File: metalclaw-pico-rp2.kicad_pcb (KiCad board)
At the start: 4 copper layers, 21 x 51 mm, 75 parts, among them J1 USB_C_Receptacle_USB2.0_14P, J2 Conn_01x05, J3 Conn_02x05_Odd_Even, J4 Conn_Coaxial, SW1 SW_Push, SW2 SW_Push, U1 ESP32-S2, U2 MX25L3236FM2I-08G-TR, U3 APS6404L-3SQRx-SN, U4 RP2350B, U5 XC6220B331MR, Y1 XRCGB40M000F1S2FR0

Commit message: Fill in BOM component details
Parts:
- removed the C19 at (157.1, 96.3)
- removed the C2 at (170.2, 92.5)
- removed J4: Conn_Coaxial, Connector_Coaxial:U.FL_Hirose_U.FL-R-SMT-1_Vertical
- removed the R17 at (157.8, 108.4)
- removed the R32 at (168.0, 116.1)
- removed the R33 at (166.6, 115.4)
- removed the R34 at (166.6, 116.7)
- removed the R35 at (168.0, 117.4)
- removed the R36 at (157.8, 110.5)
- removed the R37 at (170.2, 122.3)
- removed the R38 at (166.6, 118.1)
- removed the R39 at (157.7, 112.9)
- removed the R40 at (157.7, 115.2)
- removed U4: RP2350B, Package_DFN_QFN:QFN-80-1EP_10x10mm_P0.4mm_EP3.4x3.4mm
- added C14: 4.7u, Capacitor_SMD:C_0402_1005Metric, F.Cu at (196.6, 107.3)
- added C15: 100n, Capacitor_SMD:C_0201_0603Metric, F.Cu at (183.8, 99.7)
- added C22: 4.7u, Capacitor_SMD:C_0402_1005Metric, F.Cu at (196.6, 109.2)
- added C4: 1u, Capacitor_SMD:C_0201_0603Metric, F.Cu at (183.8, 87.5)
- added C5: 1u, Capacitor_SMD:C_0201_0603Metric, F.Cu at (183.8, 89.2)
- added C7: 1u, Capacitor_SMD:C_0201_0603Metric, F.Cu at (183.8, 91.0)
- added C8: 1u, Capacitor_SMD:C_0201_0603Metric, F.Cu at (183.8, 92.7)
- added C9: 1u, Capacitor_SMD:C_0201_0603Metric, F.Cu at (183.8, 94.5)
- added JP1: Jumper_2_Bridged, Jumper:SolderJumper-2_P1.3mm_Bridged2Bar_Pad1.0x1.5mm, F.Cu at (197.4, 112.0)
- added R1: 5.1k, Resistor_SMD:R_0201_0603Metric, F.Cu at (186.2, 87.5)
- added R10: 5.1k, Resistor_SMD:R_0201_0603Metric, F.Cu at (188.7, 87.5)
- added R11: 5.1k, Resistor_SMD:R_0201_0603Metric, F.Cu at (188.7, 89.2)
- added R12: 5.1k, Resistor_SMD:R_0201_0603Metric, F.Cu at (188.7, 91.0)
- added R13: 5.1k, Resistor_SMD:R_0201_0603Metric, F.Cu at (188.7, 92.7)
- added R14: 5.1k, Resistor_SMD:R_0201_0603Metric, F.Cu at (188.7, 94.5)
- added R15: 5.1k, Resistor_SMD:R_0201_0603Metric, F.Cu at (188.7, 96.2)
- added R18: 5.1k, Resistor_SMD:R_0201_0603Metric, F.Cu at (188.7, 99.7)
- added R2: 5.1k, Resistor_SMD:R_0201_0603Metric, F.Cu at (186.2, 89.2)
- added R20: 5.1k, Resistor_SMD:R_0201_0603Metric, F.Cu at (188.7, 101.5)
- added R21: 5.1k, Resistor_SMD:R_0201_0603Metric, F.Cu at (191.1, 87.5)
- added R22: 5.1k, Resistor_SMD:R_0201_0603Metric, F.Cu at (191.1, 89.2)
- added R23: 5.1k, Resistor_SMD:R_0201_0603Metric, F.Cu at (191.1, 91.0)
- added R24: 5.1k, Resistor_SMD:R_0201_0603Metric, F.Cu at (191.1, 92.7)
- added R25: 5.1k, Resistor_SMD:R_0201_0603Metric, F.Cu at (191.1, 94.5)
- added R26: 5.1k, Resistor_SMD:R_0201_0603Metric, F.Cu at (191.1, 96.2)
- added R27: 5.1k, Resistor_SMD:R_0201_0603Metric, F.Cu at (191.1, 98.0)
- added R29: 5.1k, Resistor_SMD:R_0201_0603Metric, F.Cu at (191.1, 101.5)
- added R3: 5.1k, Resistor_SMD:R_0201_0603Metric, F.Cu at (186.2, 91.0)
- added R4: 5.1k, Resistor_SMD:R_0201_0603Metric, F.Cu at (186.2, 92.7)
- added R5: 5.1k, Resistor_SMD:R_0201_0603Metric, F.Cu at (186.2, 94.5)
- added R55: 220, Resistor_SMD:R_0201_0603Metric, F.Cu at (193.6, 91.0)
- added R56: 220, Resistor_SMD:R_0201_0603Metric, F.Cu at (193.6, 92.7)
- added R57: 220, Resistor_SMD:R_0201_0603Metric, F.Cu at (193.6, 94.5)
- added R58: 220, Resistor_SMD:R_0201_0603Metric, F.Cu at (193.6, 96.2)
- added R59: 220, Resistor_SMD:R_0201_0603Metric, F.Cu at (193.6, 98.0)
- added R6: 5.1k, Resistor_SMD:R_0201_0603Metric, F.Cu at (186.2, 96.2)
- added R60: 220, Resistor_SMD:R_0201_0603Metric, F.Cu at (193.6, 99.7)
- added R61: 220, Resistor_SMD:R_0201_0603Metric, F.Cu at (193.6, 101.5)
- added R62: 220, Resistor_SMD:R_0201_0603Metric, F.Cu at (196.0, 87.5)
- added R63: 220, Resistor_SMD:R_0201_0603Metric, F.Cu at (196.0, 89.2)
- added R64: 220, Resistor_SMD:R_0201_0603Metric, F.Cu at (196.0, 91.0)
- added R65: 220, Resistor_SMD:R_0201_0603Metric, F.Cu at (196.0, 92.7)
- added R66: 220, Resistor_SMD:R_0201_0603Metric, F.Cu at (196.0, 94.5)
- added R67: 220, Resistor_SMD:R_0201_0603Metric, F.Cu at (196.0, 96.2)
- added R68: 220, Resistor_SMD:R_0201_0603Metric, F.Cu at (196.0, 98.0)
- added R69: 220, Resistor_SMD:R_0201_0603Metric, F.Cu at (196.0, 99.7)
- added R7: 5.1k, Resistor_SMD:R_0201_0603Metric, F.Cu at (186.2, 98.0)
- added R70: 220, Resistor_SMD:R_0201_0603Metric, F.Cu at (196.0, 101.5)
- added R71: 220, Resistor_SMD:R_0201_0603Metric, F.Cu at (198.5, 87.5)
- added R72: 220, Resistor_SMD:R_0201_0603Metric, F.Cu at (198.5, 89.2)
- added R73: 220, Resistor_SMD:R_0201_0603Metric, F.Cu at (198.5, 91.0)
- added R74: 220, Resistor_SMD:R_0201_0603Metric, F.Cu at (198.5, 92.7)
- added R75: 220, Resistor_SMD:R_0201_0603Metric, F.Cu at (198.5, 94.5)
- added R76: 220, Resistor_SMD:R_0201_0603Metric, F.Cu at (198.5, 96.2)
- added R79: 33, Resistor_SMD:R_0402_1005Metric, F.Cu at (199.5, 106.7)
- added R80: 5.1k, Resistor_SMD:R_0201_0603Metric, F.Cu at (198.5, 98.0)
- added R81: 5.1k, Resistor_SMD:R_0201_0603Metric, F.Cu at (198.5, 99.7)
- added R82: 5.1k, Resistor_SMD:R_0201_0603Metric, F.Cu at (198.5, 101.5)
- added R9: 5.1k, Resistor_SMD:R_0201_0603Metric, F.Cu at (186.2, 101.5)
- C11: value 1u -> 100n; footprint Capacitor_SMD:C_0201_0603Metric -> Capacitor_SMD:C_0402_1005Metric
- C12: value C -> 1u
- C13: value C -> 4.7u; footprint Capacitor_SMD:C_0201_0603Metric -> Capacitor_SMD:C_0402_1005Metric
- C16: value 1u -> 100n
- C24: renamed from C5; value 6p -> 15p; footprint Capacitor_SMD:C_0201_0603Metric -> Capacitor_SMD:C_0402_1005Metric
- C25: renamed from C6; value 6p -> 15p; footprint Capacitor_SMD:C_0201_0603Metric -> Capacitor_SMD:C_0402_1005Metric
- L1: value L -> 3.3u; footprint Inductor_SMD:L_0201_0603Metric -> Inductor_SMD_Wurth:L_Wurth_WE-LQSH-2010
- R16, R28, R8: value 220 -> 5.1k
- U2: value MX25L3236FM2I-08G-TR -> RP2354B; footprint Package_SO:SOIC-8_5.3x5.3mm_P1.27mm -> Package_DFN_QFN:QFN-80-1EP_10x10mm_P0.4mm_EP3.4x3.4mm
- Y1: value XRCGB40M000F1S2FR0 -> ABM8-272-T3; footprint Crystal:Crystal_SMD_2016-4Pin_2.0x1.6mm -> Crystal:Crystal_SMD_3225-4Pin_3.2x2.5mm
- moved R31 49.1 mm to (193.6, 89.2)
- moved L1 34.8 mm to (200.0, 104.0), turned to 0 degrees
- moved C11 33.9 mm to (196.6, 103.3), turned to 0 degrees
- moved C13 30.3 mm to (196.6, 105.3), turned to 0 degrees
- moved U2 30.2 mm to (189.1, 108.5), turned to 0 degrees
- moved R30 26.0 mm to (193.6, 87.5), turned to 0 degrees
- moved R28 22.0 mm to (191.1, 99.7)
- moved C12 21.5 mm to (183.8, 98.0), turned to 0 degrees
- moved C10 19.9 mm to (183.8, 96.2), turned to 0 degrees
- moved C16 18.8 mm to (183.8, 101.5), turned to 0 degrees
- moved R16 18.4 mm to (188.7, 98.0), turned to 0 degrees
- moved R8 15.9 mm to (186.2, 99.7), turned to 0 degrees
- renumbered A2 to A1, C15 to C17, C14 to C18, C9 to C19, C3 to C2, C8 to C20, C7 to C21, C4 to C23, C18 to C26, C17 to C6, J3 to J2, R41 to R17, R42 to R19, R2 to R32, R3 to R33, R4 to R34, R5 to R35, R6 to R36, R7 to R37, R18 to R38, R19 to R39, R20 to R40, R21 to R41, R22 to R42, R23 to R43, R24 to R44, R25 to R45, R26 to R46, R27 to R47, R15 to R48, R14 to R49, R13 to R50, R12 to R51, R11 to R52, R10 to R53, R9 to R54, R1 to R77, R29 to R78, SW2 to SW1, SW1 to SW2, U5 to U1
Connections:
- A1 pad 1: Net-(A2-GPIO0) -> /GP0
- A1 pad 10: Net-(A2-GPIO7) -> /GP7
- A1 pad 11: Net-(A2-GPIO8) -> /GP8
- A1 pad 12: Net-(A2-GPIO9) -> /GP9
- A1 pad 14: Net-(A2-GPIO10) -> /GP10
- A1 pad 15: Net-(A2-GPIO11) -> /GP11
- A1 pad 16: Net-(A2-GPIO12) -> /GP12
- A1 pad 17: Net-(A2-GPIO13) -> /GP13
- A1 pad 19: Net-(A2-GPIO14) -> /GP14
- A1 pad 2: Net-(A2-GPIO1) -> /GP1
- A1 pad 20: Net-(A2-GPIO15) -> /GP15
- A1 pad 21: Net-(A2-GPIO16) -> /GP16
- A1 pad 22: Net-(A2-GPIO17) -> /GP17
- A1 pad 24: Net-(A2-GPIO18) -> /GP18
- A1 pad 25: Net-(A2-GPIO19) -> /GP19
- A1 pad 26: Net-(A2-GPIO20) -> /GP20
- A1 pad 27: Net-(A2-GPIO21) -> /GP21
- A1 pad 29: Net-(A2-GPIO22) -> /GP22
- A1 pad 31: Net-(A2-GPIO26_ADC0) -> Net-(A1-GPIO26_ADC0)
- A1 pad 32: Net-(A2-GPIO27_ADC1) -> Net-(A1-GPIO27_ADC1)
- A1 pad 33: GND -> Net-(A1-AGND)
- A1 pad 34: /GP28 -> Net-(A1-GPIO28_ADC2)
- A1 pad 35: +3V3 -> unconnected-(A1-ADC_VREF-Pad35)
- A1 pad 36: unconnected-(A2-3V3-Pad36) -> +3.3VP
- A1 pad 39: unconnected-(A2-VSYS-Pad39) -> VS
- A1 pad 4: Net-(A2-GPIO2) -> /GP2
- A1 pad 40: VBUS -> unconnected-(A1-VBUS-Pad40)
- A1 pad 5: Net-(A2-GPIO3) -> /GP3
- A1 pad 6: Net-(A2-GPIO4) -> /GP4
- A1 pad 7: Net-(A2-GPIO5) -> /GP5
- A1 pad 9: Net-(A2-GPIO6) -> /GP6
- C10 pad 1: +3V3 -> GND
- C10 pad 2: GND -> Net-(C10-Pad2)
- C11 pad 1: +3V3 -> GND
- C11 pad 2: GND -> Net-(U2-VREG_AVDD)
- C12 pad 1: Net-(U1-LNA_IN) -> GND
- C12 pad 2: GND -> +3V3
- C13 pad 1: Net-(J4-In) -> GND
- C13 pad 2: GND -> +3V3
- C16 pad 1: Net-(C16-Pad1) -> GND
- C16 pad 2: /3V3_EN -> +3V3
- C17 pad 1: +3V3 -> GND
- C17 pad 2: GND -> +3V3
- C18 pad 1: +3V3 -> GND
- C18 pad 2: GND -> +3V3
- C19 pad 1: +3V3 -> GND
- C19 pad 2: GND -> +3V3
- C20 pad 1: +3V3 -> GND
- C20 pad 2: GND -> +3V3
- C21 pad 1: +3V3 -> GND
- C21 pad 2: GND -> Net-(U2-VREG_FB)
- C23 pad 1: +3V3 -> GND
- C23 pad 2: GND -> +3V3
- C24 pad 1: Net-(U1-XTAL_P) -> Net-(U2-XIN)
- C25 pad 1: Net-(U1-XTAL_N) -> GND
- C25 pad 2: GND -> Net-(U2-XOUT)
- C26 pad 1: GND -> +3V3
- C26 pad 2: VDD -> GND
- C6 pad 1: Net-(C17-Pad1) -> GND
- J1 pad A6: /USB_D+ -> Net-(J1-D+-PadA6)
- J1 pad A7: /USB_D- -> Net-(J1-D--PadA7)
- J1 pad B6: /USB_D+ -> Net-(J1-D+-PadA6)
- J1 pad B7: /USB_D- -> Net-(J1-D--PadA7)
- J1 pad S1: unconnected-(J1-SHIELD-PadS1) -> GND
- J2 pad 10: unconnected-(J3-Pin_10-Pad10) -> /RESET
- J2 pad 2: /MTMS -> Net-(J2-Pin_2)
- J2 pad 4: /MTCK -> Net-(J2-Pin_4)
- J2 pad 6: /MTDO -> unconnected-(J2-Pin_6-Pad6)
- J2 pad 7: GND -> unconnected-(J2-Pin_7-Pad7)
- J2 pad 8: /MTDI -> unconnected-(J2-Pin_8-Pad8)
- L1 pad 1: Net-(U1-LNA_IN) -> Net-(U2-VREG_FB)
- L1 pad 2: Net-(J4-In) -> Net-(U2-VREG_LX)
- R16 pad 1: Net-(A2-GPIO27_ADC1) -> +3.3VP
- R16 pad 2: /GP27 -> /GP8
- R17 pad 2: /3V3_EN -> /BOOTSEL
- R28 pad 1: Net-(U1-GPIO21) -> /GP16
- R28 pad 2: /GP28 -> +3.3VP
- R30 pad 1: GND -> /GP27
- R30 pad 2: /RUN -> Net-(C9-Pad2)
- R31 pad 1: GND -> /GP28
- R31 pad 2: /GP15 -> Net-(C10-Pad2)
- R32 pad 1: Net-(A2-GPIO0) -> /GP3
- R32 pad 2: /GP0 -> Net-(U2-GPIO0)
- R33 pad 1: Net-(A2-GPIO1) -> /3V3_EN
- R33 pad 2: /GP1 -> Net-(U2-GPIO1)
- R34 pad 1: Net-(A2-GPIO2) -> /GP1
- R34 pad 2: /GP2 -> Net-(U2-GPIO2)
- R35 pad 1: Net-(A2-GPIO3) -> /GP0
- R35 pad 2: /GP3 -> Net-(U2-GPIO3)
- R36 pad 1: Net-(A2-GPIO4) -> /GP0
- R36 pad 2: /GP4 -> Net-(U2-GPIO4)
- R37 pad 1: Net-(A2-GPIO5) -> /GP1
- R37 pad 2: /GP5 -> Net-(U2-GPIO5)
- R38 pad 1: Net-(A2-GPIO6) -> /GP2
- R38 pad 2: /GP6 -> Net-(U2-GPIO6)
- R39 pad 1: Net-(A2-GPIO7) -> /GP3
- R39 pad 2: /GP7 -> Net-(U2-GPIO7)
- R40 pad 1: Net-(A2-GPIO8) -> /GP7
- R40 pad 2: /GP8 -> Net-(U2-GPIO8)
- R41 pad 1: Net-(A2-GPIO9) -> /RUN
- R41 pad 2: /GP9 -> Net-(U2-GPIO9)
- R42 pad 1: Net-(A2-GPIO10) -> /GP5
- R42 pad 2: /GP10 -> Net-(U2-GPIO10)
- R43 pad 1: Net-(A2-GPIO11) -> /GP4
- R43 pad 2: /GP11 -> Net-(U2-GPIO11)
- R44 pad 1: Net-(A2-GPIO12) -> /GP4
- R44 pad 2: /GP12 -> Net-(U2-GPIO12)
- R45 pad 1: Net-(A2-GPIO13) -> /GP5
- R45 pad 2: /GP13 -> Net-(U2-GPIO13)
- R46 pad 1: Net-(A2-GPIO14) -> /GP6
- R46 pad 2: /GP14 -> Net-(U2-GPIO14)
- R47 pad 1: Net-(A2-GPIO15) -> /GP7
- R47 pad 2: /GP15 -> Net-(U2-GPIO15)
- R48 pad 1: Net-(A2-GPIO16) -> /GP11
- R48 pad 2: /GP16 -> Net-(U2-GPIO16)
- R49 pad 1: Net-(A2-GPIO17) -> /SWCLK
- R49 pad 2: /GP17 -> Net-(U2-GPIO17)
- R50 pad 1: Net-(A2-GPIO18) -> /GP9
- R50 pad 2: /GP18 -> Net-(U2-GPIO18)
- R51 pad 1: Net-(A2-GPIO19) -> /GP8
- R51 pad 2: /GP19 -> Net-(U2-GPIO19)
- R52 pad 1: Net-(A2-GPIO20) -> /GP8
- R52 pad 2: /GP20 -> Net-(U2-GPIO20)
- R53 pad 1: Net-(A2-GPIO21) -> /GP9
- R53 pad 2: /GP21 -> Net-(U2-GPIO21)
- R54 pad 1: Net-(A2-GPIO22) -> /GP10
- R54 pad 2: /GP22 -> Net-(U2-GPIO22)
- R8 pad 1: Net-(A2-GPIO26_ADC0) -> +3.3VP
- R8 pad 2: /GP26 -> /GP12
- SW1 pad 2: Net-(C16-Pad1) -> Net-(R80-Pad2)
- SW2 pad 2: Net-(C17-Pad1) -> /RESET
- U2 pad 1: Net-(U1-SPICS0) -> Net-(U2-GPIO4)
- U2 pad 2: Net-(U1-SPIQ) -> Net-(U2-GPIO5)
- U2 pad 3: Net-(U1-SPIWP) -> Net-(U2-GPIO6)
- U2 pad 4: GND -> Net-(U2-GPIO7)
- U2 pad 5: Net-(U1-SPID) -> +3V3
- U2 pad 6: Net-(U1-SPICLK) -> Net-(U2-GPIO8)
- U2 pad 7: Net-(U1-SPIHD) -> Net-(U2-GPIO9)
- U2 pad 8: VDD -> Net-(U2-GPIO10)
- U3 pad 1: Net-(U1-SPICS1) -> Net-(U2-GPIO47/ADC7)
- U3 pad 2: Net-(U1-SPIQ) -> Net-(U2-QSPI_SD1)
- U3 pad 3: Net-(U1-SPIWP) -> Net-(U2-QSPI_SD2)
- U3 pad 5: Net-(U1-SPID) -> Net-(U2-QSPI_SD0)
- U3 pad 6: Net-(U1-SPICLK) -> Net-(U2-QSPI_SCLK)
- U3 pad 7: Net-(U1-SPIHD) -> Net-(U2-QSPI_SD3)
- U3 pad 8: VDD -> +3V3
- Y1 pad 1: Net-(U1-XTAL_N) -> Net-(U2-XIN)
- Y1 pad 3: Net-(U1-XTAL_P) -> Net-(U2-XOUT)
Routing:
- net (no net): track 0.00 -> 52.2 mm
- net Net-(U2-GPIO0): track 0.00 -> 46.5 mm, vias 0 -> 2
- net /GP0: track 49.6 -> 3.10 mm, vias 2 -> 0
- net Net-(J1-D--PadA7): track 0.00 -> 15.3 mm, vias 0 -> 1
- net /USB_D-: track 15.3 -> 0.00 mm, vias 1 -> 0
- net Net-(J1-D+-PadA6): track 0.00 -> 14.6 mm, vias 0 -> 1
- net /USB_D+: track 14.6 -> 0.00 mm, vias 1 -> 0
- net /GP21: track 13.8 -> 20.9 mm
- net Net-(A2-GPIO21): track 7.11 -> 0.00 mm
- net Net-(A2-GPIO17): track 5.36 -> 0.00 mm
- net Net-(U2-GPIO22): track 0.00 -> 4.87 mm, vias 0 -> 2
- net /GP22: track 7.84 -> 2.98 mm, vias 2 -> 0
- net Net-(A1-GPIO28_ADC2): track 0.00 -> 4.80 mm
- net /GP28: track 4.80 -> 0.00 mm
- net Net-(A2-GPIO14): track 4.16 -> 0.00 mm
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
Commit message: Rip out outdated footprints from layout
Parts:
- removed the J2 at (158.7, 120.2)
- removed the U1 at (163.8, 102.7)
- added C27: 100n, Capacitor_SMD:C_0402_1005Metric, F.Cu at (211.9, 108.4)
- added C28: 100n, Capacitor_SMD:C_0402_1005Metric, F.Cu at (211.9, 110.4)
- added C3: 100n, Capacitor_SMD:C_0402_1005Metric, F.Cu at (211.9, 106.5)
- added D1: PMEG2010ER,115, Diode_SMD:Nexperia_CFP3_SOD-123W, F.Cu at (216.1, 107.1)
- added R83: 1k, Resistor_SMD:R_0402_1005Metric, F.Cu at (214.8, 109.7)
- C10, C8, C9: value 1u -> 10n; footprint Capacitor_SMD:C_0201_0603Metric -> Capacitor_SMD:C_0402_1005Metric
- C11: value 100n -> 4.7u
- C12, C15, C16, C17, C18, C19, C20, C21, C23, C26: footprint Capacitor_SMD:C_0201_0603Metric -> Capacitor_SMD:C_0402_1005Metric
- C4, C5, C7: value 1u -> 1.5n; footprint Capacitor_SMD:C_0201_0603Metric -> Capacitor_SMD:C_0402_1005Metric
- C6: value 1u -> 100n; footprint Capacitor_SMD:C_0201_0603Metric -> Capacitor_SMD:C_0402_1005Metric
- J1: value USB_C_Receptacle_USB2.0_14P -> USB4105-GF-A
- J2: value Conn_02x05_Odd_Even -> FTSH-105-01-L-DV-K
- R1, R10, R11, R12, R13, R14, R15, R16, R17, R18, R19, R2, R20, R21, R24, R26, R27, R28, R3, R4, R5, R6, R7, R77, R78, R8, R9: footprint Resistor_SMD:R_0201_0603Metric -> Resistor_SMD:R_0402_1005Metric
- R22, R23, R25: value 5.1k -> 2.2k; footprint Resistor_SMD:R_0201_0603Metric -> Resistor_SMD:R_0402_1005Metric
- R29, R30, R31: value 5.1k -> 330; footprint Resistor_SMD:R_0201_0603Metric -> Resistor_SMD:R_0402_1005Metric
- R32, R34, R35, R36, R37, R38, R39, R40, R42, R43, R44, R45, R46, R47, R48, R49, R50, R51, R52, R53, R54, R55, R56, R57, R58, R59, R60, R61, R62, R63, R64, R65, R66, R67, R68, R69, R70, R71, R72, R73, R74, R75: value 220 -> 33; footprint Resistor_SMD:R_0201_0603Metric -> Resistor_SMD:R_0402_1005Metric
- R33, R41: value 220 -> 1k; footprint Resistor_SMD:R_0201_0603Metric -> Resistor_SMD:R_0402_1005Metric
- R76: value 220 -> 10k; footprint Resistor_SMD:R_0201_0603Metric -> Resistor_SMD:R_0402_1005Metric
- R80: value 5.1k -> 1k; footprint Resistor_SMD:R_0201_0603Metric -> Resistor_SMD:R_0402_1005Metric
- R81, R82: value 5.1k -> 27; footprint Resistor_SMD:R_0201_0603Metric -> Resistor_SMD:R_0402_1005Metric
- SW1, SW2: value SW_Push -> PTS810SJM250SMTR LFS
- U1: value XC6220B331MR -> XC6220B331MR-G
- U3: value APS6404L-3SQRx-SN -> APS6404L-3SQR-SN
- moved C18 41.5 mm to (125.6, 106.0)
- moved C21 41.5 mm to (124.4, 95.6)
- moved R17 41.5 mm to (129.1, 85.0)
- moved R36 41.5 mm to (115.6, 85.3)
- moved R38 41.5 mm to (115.6, 93.0)
- moved R43 41.5 mm to (115.6, 108.8)
- moved R49 41.5 mm to (127.1, 116.4)
- moved R50 41.5 mm to (128.5, 115.9)
- moved R51 41.5 mm to (128.5, 115.0)
- moved R53 41.5 mm to (127.1, 113.7)
- moved R54 41.5 mm to (129.1, 100.6)
- moved C17 41.5 mm to (116.9, 104.9)
- moved C20 41.5 mm to (117.3, 98.4)
- moved C24 41.5 mm to (120.9, 107.8)
- moved C26 41.5 mm to (116.3, 88.5)
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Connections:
- C1 pad 1: VBUS -> VS
- C25 pad 2: Net-(U2-XOUT) -> Net-(C25-Pad2)
- J1 pad A4: VBUS -> Net-(D1-A)
- J1 pad A9: VBUS -> Net-(D1-A)
- J1 pad B4: VBUS -> Net-(D1-A)
- J1 pad B9: VBUS -> Net-(D1-A)
- U1 pad 1: VBUS -> VS
- U1 pad 3: VBUS -> VS
- Y1 pad 3: Net-(U2-XOUT) -> Net-(C25-Pad2)
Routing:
- net (no net): track 52.2 -> 0.00 mm
- net /GP3: track 48.3 -> 0.00 mm, vias 4 -> 0
- net /GP4: track 47.8 -> 0.00 mm, vias 4 -> 0
- net /GP1: track 47.0 -> 0.00 mm, vias 2 -> 0
- net Net-(U2-GPIO0): track 46.5 -> 0.00 mm, vias 2 -> 0
- net /GP2: track 43.8 -> 0.00 mm, vias 2 -> 0
- net /GP7: track 37.7 -> 0.00 mm, vias 4 -> 0
- net /GP6: track 36.9 -> 0.00 mm, vias 4 -> 0
- net /GP5: track 34.6 -> 0.00 mm, vias 4 -> 0
- net /RUN: track 33.3 -> 0.00 mm, vias 1 -> 0
- net /GP8: track 31.1 -> 0.00 mm, vias 4 -> 0
- net /GP16: track 23.2 -> 0.00 mm, vias 1 -> 0
- net /GP18: track 21.2 -> 0.00 mm, vias 2 -> 0
- net /GP21: track 20.9 -> 0.00 mm, vias 1 -> 0
- net /GP17: track 18.0 -> 0.00 mm, vias 2 -> 0
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
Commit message: Switch to smaller footprints
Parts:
- C10, C15, C16, C17, C18, C19, C20, C21, C23, C24, C25, C27, C28, C3, C6, C8, C9: footprint Capacitor_SMD:C_0402_1005Metric -> Capacitor_SMD:C_0201_0603Metric
- JP1: moved to B.Cu
- R1, R10, R11, R12, R13, R14, R15, R16, R17, R18, R19, R2, R20, R21, R22, R23, R24, R25, R26, R27, R28, R29, R3, R30, R31, R33, R4, R41, R5, R6, R7, R76, R77, R78, R8, R80, R81, R82, R83, R9: footprint Resistor_SMD:R_0402_1005Metric -> Resistor_SMD:R_0201_0603Metric
- R32, R34, R35, R36, R37, R38, R39, R40, R42, R43, R44, R45, R46, R47, R48, R49, R50, R51, R52, R53, R54, R55, R56, R57, R58, R59, R60, R61, R62, R63, R64, R65, R66, R67, R68, R69, R70, R71, R72, R73, R74, R75: value 33 -> 100; footprint Resistor_SMD:R_0402_1005Metric -> Resistor_SMD:R_0201_0603Metric
- moved D1 54.9 mm to (170.1, 77.2), turned to 90 degrees
- moved R36 43.0 mm to (157.6, 76.1), turned to 0 degrees
- moved R35 42.8 mm to (157.6, 75.1), turned to 0 degrees
- moved R15 38.2 mm to (157.6, 74.1)
- moved U2 27.3 mm to (163.7, 98.3)
- moved J2 24.6 mm to (163.6, 116.4)
- turned JP1 to 180 degrees

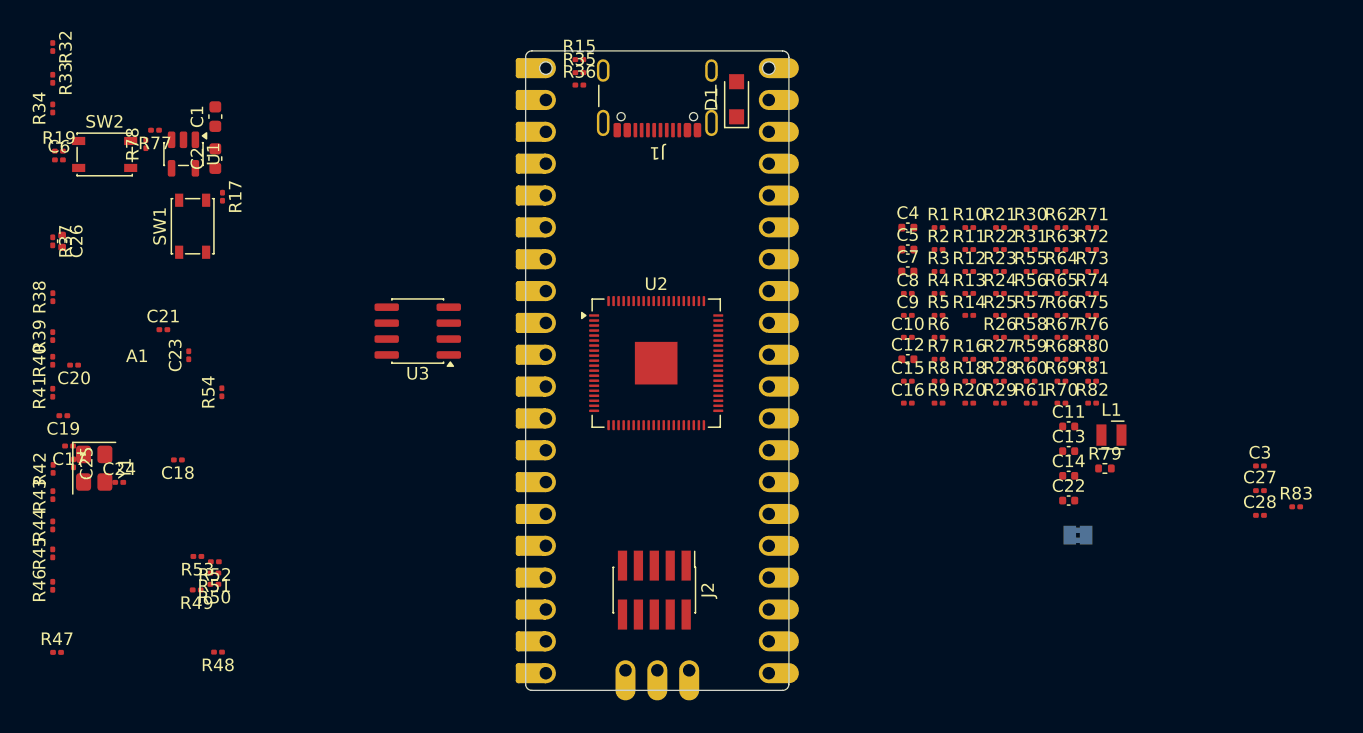
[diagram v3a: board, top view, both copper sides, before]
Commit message: Move resistors to their rough placements
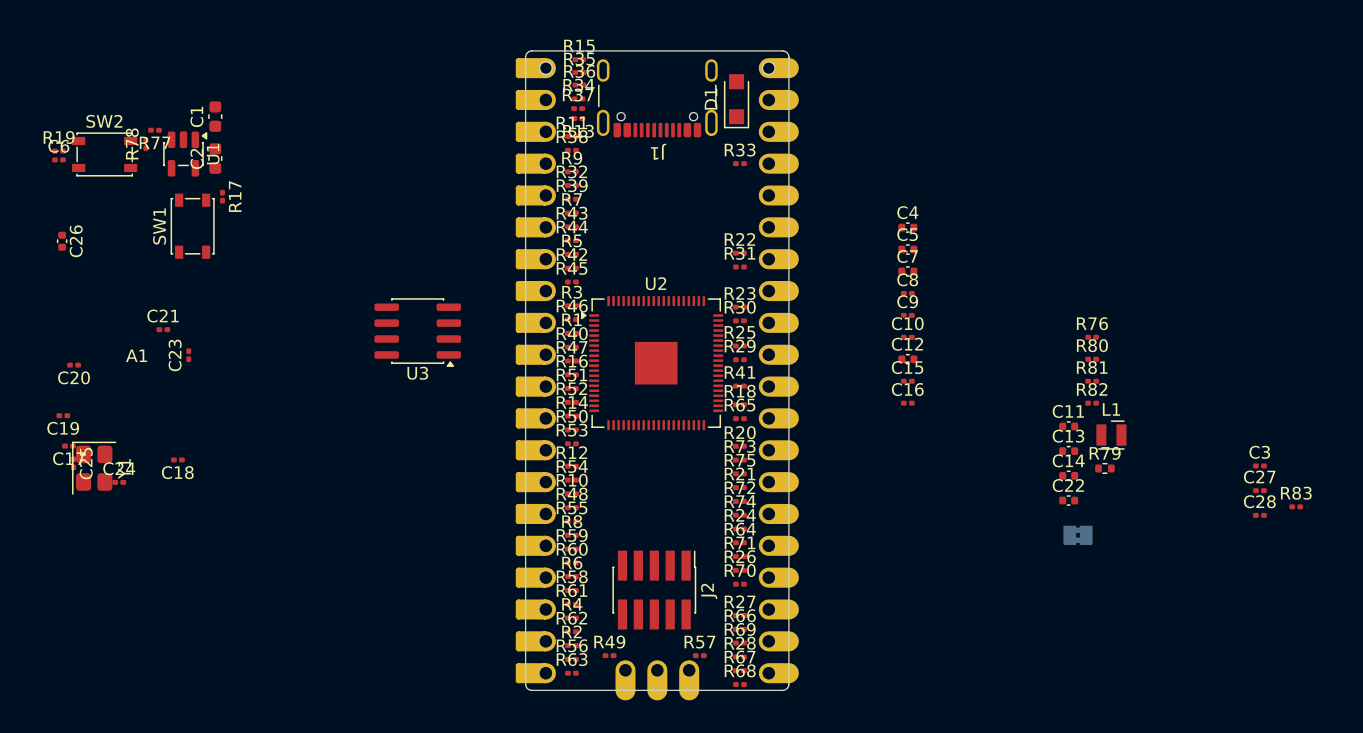
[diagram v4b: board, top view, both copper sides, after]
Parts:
- moved R33 55.2 mm to (170.4, 82.4), turned to 0 degrees
- moved R41 54.8 mm to (170.4, 100.1), turned to 0 degrees
- moved R63 51.6 mm to (157.0, 123.0)
- moved R62 50.6 mm to (157.0, 119.7)
- moved R44 47.2 mm to (157.0, 88.5), turned to 0 degrees
- moved R47 47.2 mm to (157.0, 98.1)
- moved R56 46.8 mm to (157.0, 121.9)
- moved R45 46.7 mm to (157.0, 91.8), turned to 0 degrees
- moved R43 46.6 mm to (157.0, 87.4), turned to 0 degrees
- moved R46 46.5 mm to (157.0, 94.8), turned to 0 degrees
- moved R42 44.4 mm to (157.0, 90.7), turned to 0 degrees
- moved R37 43.2 mm to (157.5, 78.0), turned to 0 degrees
- moved R2 43.0 mm to (157.0, 120.8)
- moved R38 43.0 mm to (157.0, 81.3), turned to 0 degrees
- moved R32 42.9 mm to (157.0, 84.1), turned to 0 degrees
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
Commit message: Move more components to their rough placements
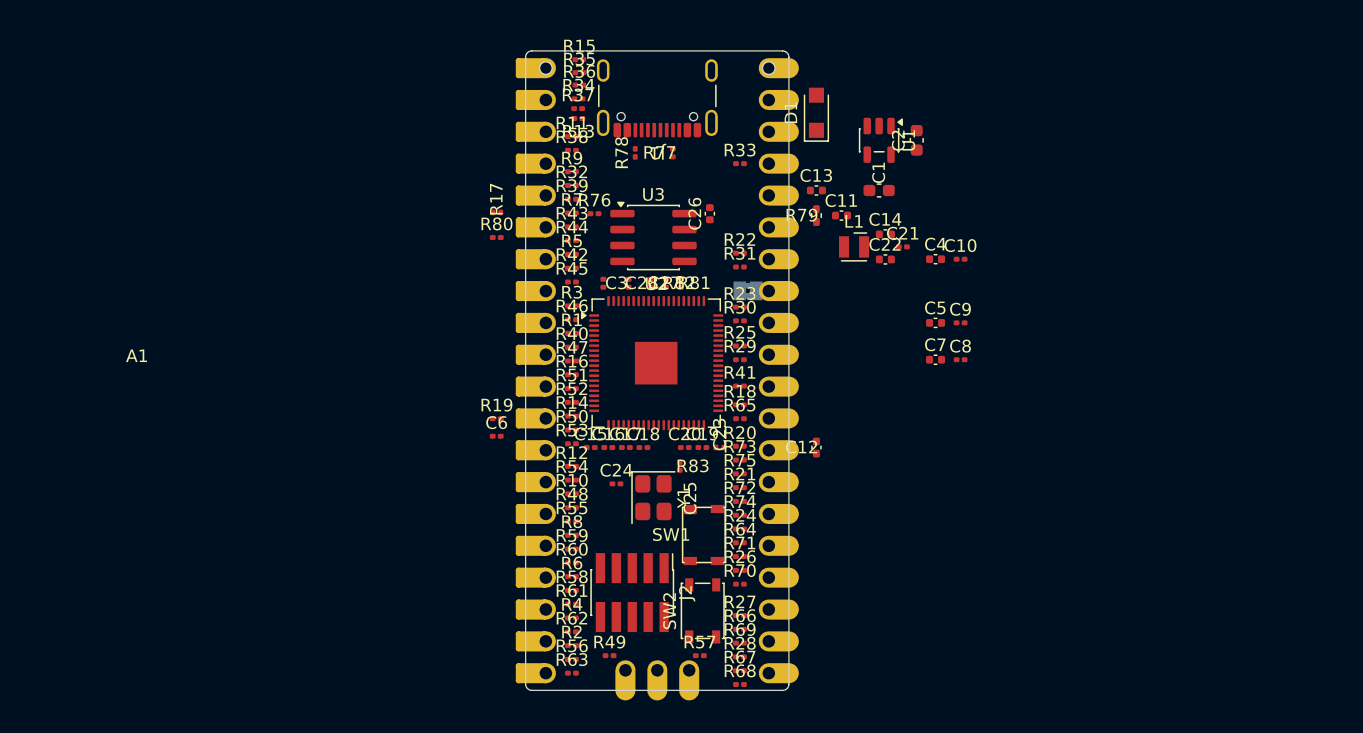
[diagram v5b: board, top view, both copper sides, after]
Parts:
- moved SW2 60.0 mm to (167.4, 118.0), turned to 90 degrees
- moved C21 59.4 mm to (183.4, 89.0)
- moved C2 56.0 mm to (184.5, 80.5)
- moved U1 55.5 mm to (181.5, 80.5)
- moved C3 54.4 mm to (159.5, 91.9), turned to -90 degrees
- moved C28 53.6 mm to (161.5, 91.9), turned to -90 degrees
- moved C1 53.3 mm to (181.5, 84.5), turned to 0 degrees
- moved C26 51.7 mm to (168.0, 86.3), turned to 90 degrees
- moved C27 51.3 mm to (163.3, 91.9), turned to -90 degrees
- moved C19 51.0 mm to (167.4, 105.0), turned to 0 degrees
- moved C25 49.4 mm to (166.4, 110.1), turned to 0 degrees
- moved R83 49.3 mm to (165.6, 106.5), turned to -90 degrees
- moved C20 49.2 mm to (166.0, 105.0), turned to 0 degrees
- moved R80 48.5 mm to (151.0, 88.2)
- moved SW1 47.6 mm to (167.5, 112.0)
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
